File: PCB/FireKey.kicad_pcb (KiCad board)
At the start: 2 copper layers, 100 x 96.5 mm, 75 parts, among them SW1 SW_MEC_4A, U1 Arduino_Pro_Micro_USB-C

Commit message: Worked on V1.0.0 PCB
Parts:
- removed C15: 100nF, Capacitor_SMD:C_0603_1608Metric_Pad1.08x0.95mm_HandSolder
- removed G1: FireKey_Logo, Custom_Parts:FireKey_Logo
- removed H11, H12: M3_Hole, MountingHole:MountingHole_3.2mm_M3
- removed LED15: DY-S352818, Custom_Parts:DY-S352818-6812-2T
- added C0: 100nF, Capacitor_SMD:C_0603_1608Metric_Pad1.08x0.95mm_HandSolder, B.Cu at (231.5, 91.3)
- added LED0: SK6812, Custom_Parts:DY-S352818-6812-2T, B.Cu at (238.8, 92.1)
- added Logo1: Logo_FireKey, Custom_FireKey:Logo_FireKey_32x9.4, F.Cu at (128.9, 162.4)
- added OLED2: OLED_1.3_4P, Custom_Module:OLED_1.3_4P_withM2.5Holes, F.Cu at (207.8, 55.9)
- H1: renamed from H5; value M3_Hole -> M2.5_Hole; footprint MountingHole:MountingHole_3.2mm_M3 -> MountingHole:MountingHole_2.7mm_M2.5
- H2: renamed from H6; value M3_Hole -> M2.5_Hole; footprint MountingHole:MountingHole_3.2mm_M3 -> MountingHole:MountingHole_2.7mm_M2.5
- H3: renamed from H9; value M3_Hole -> M2.5_Hole; footprint MountingHole:MountingHole_3.2mm_M3 -> MountingHole:MountingHole_2.7mm_M2.5
- H4: renamed from H10; value M3_Hole -> M2.5_Hole; footprint MountingHole:MountingHole_3.2mm_M3 -> MountingHole:MountingHole_2.7mm_M2.5
- H5: renamed from H7; value M3_Hole -> M2.5_Hole; footprint MountingHole:MountingHole_3.2mm_M3 -> MountingHole:MountingHole_2.7mm_M2.5
- H6: renamed from H8; value M3_Hole -> M2.5_Hole; footprint MountingHole:MountingHole_3.2mm_M3 -> MountingHole:MountingHole_2.7mm_M2.5
- LED1, LED10, LED11, LED12, LED13, LED14, LED2, LED3, LED4, LED5, LED6, LED7, LED8, LED9: value DY-S352818 -> SK6812
- moved H2 200.3 mm to (248.9, 41.3)
- moved C9 184.9 mm to (246.0, 111.9), turned to 0 degrees
- moved KEY15 170.7 mm to (241.3, 119.4)
- moved D15 170.6 mm to (245.7, 118.1)
- moved LED10 170.3 mm to (238.8, 130.2), turned to 180 degrees
- moved LED9 170.3 mm to (238.8, 111.1), turned to 0 degrees
- moved C10 155.8 mm to (231.5, 129.4), turned to 180 degrees
- moved KEY14 154.4 mm to (241.3, 100.3)
- moved D14 154.4 mm to (245.7, 99.1)
- moved D4 151.3 mm to (226.7, 80.0)
- moved KEY4 151.3 mm to (222.2, 81.3)
- moved C8 146.8 mm to (226.9, 111.9), turned to 0 degrees
- moved KEY13 141.5 mm to (241.3, 81.3)
- moved D13 141.4 mm to (245.7, 80.0)
- moved KEY3 134.5 mm to (203.2, 81.3)
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- renumbered H3 to P1, H2 to P2
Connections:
- D10 pad 1: Row3 -> Row2
- D11 pad 1: Row3 -> Row2
- D12 pad 1: Row3 -> Row2
- D13 pad 1: Row4 -> Row0
- D14 pad 1: Row4 -> Row1
- D15 pad 1: Row4 -> Row2
- D4 pad 1: Row1 -> Row0
- D7 pad 1: Row2 -> Row1
- D8 pad 1: Row2 -> Row1
- KEY1 pad 2: Col0 -> Col4
- KEY10 pad 2: Col2 -> Col3
- KEY11 pad 2: Col1 -> Col2
- KEY12 pad 2: Col0 -> Col1
- KEY14 pad 2: Col1 -> Col0
- KEY15 pad 2: Col2 -> Col0
- KEY2 pad 2: Col1 -> Col3
- KEY4 pad 2: Col2 -> Col1
- KEY5 pad 2: Col1 -> Col4
- KEY6 pad 2: Col0 -> Col3
- KEY7 pad 2: Col0 -> Col2
- KEY9 pad 2: Col2 -> Col4
- LED1 pad 4: Net-(LED1-Pad4) -> Net-(LED0-Pad2)
- LED14 pad 2: Net-(LED14-Pad2) -> unconnected-(LED14-Pad2)
- R1 pad 1: Net-(LED1-Pad4) -> Net-(LED0-Pad4)
- U1 pad 10: Col0 -> Row0
- U1 pad 14: Col2 -> Row2
- U1 pad 16: Col1 -> Row1
- U1 pad 5: Row0 -> Col0
- U1 pad 6: Row1 -> Col1
- U1 pad 7: Row2 -> Col2
- U1 pad 8: Row3 -> Col3
- U1 pad 9: Row4 -> Col4
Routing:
- net VCC: track 575.2 -> 0.00 mm, vias 7 -> 0
- net Col2: track 189.8 -> 0.00 mm
- net Col1: track 169.2 -> 0.00 mm
- net Col0: track 144.6 -> 0.00 mm
- net Row4: track 91.8 -> 0.00 mm
- net Row3: track 73.0 -> 0.00 mm
- net Row0: track 67.2 -> 0.00 mm
- net Row2: track 58.4 -> 0.00 mm
- net Row1: track 56.4 -> 0.00 mm
- net SDA: track 46.6 -> 0.00 mm
- net LEDpin: track 45.2 -> 0.00 mm, vias 1 -> 0
- net SCL: track 42.7 -> 0.00 mm
- net Net-(LED3-Pad2): track 27.2 -> 0.00 mm
- net Net-(LED10-Pad4): track 27.2 -> 0.00 mm
- net Net-(LED6-Pad2): track 26.7 -> 0.00 mm, vias 2 -> 0
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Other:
- board size 100 x 96.5 mm -> 99.7 x 99.1 mm
- board text added: "V1.0"
- board text removed: "V0.1"

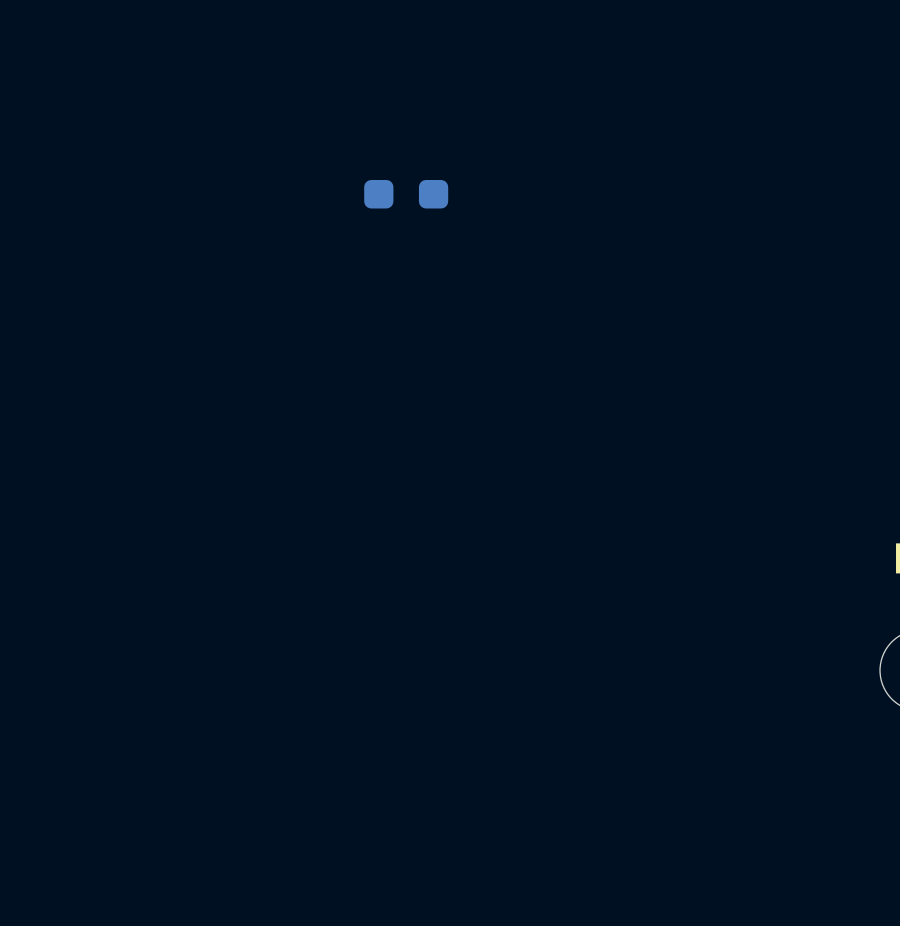
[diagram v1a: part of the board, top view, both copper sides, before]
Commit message: group key sets on pcb
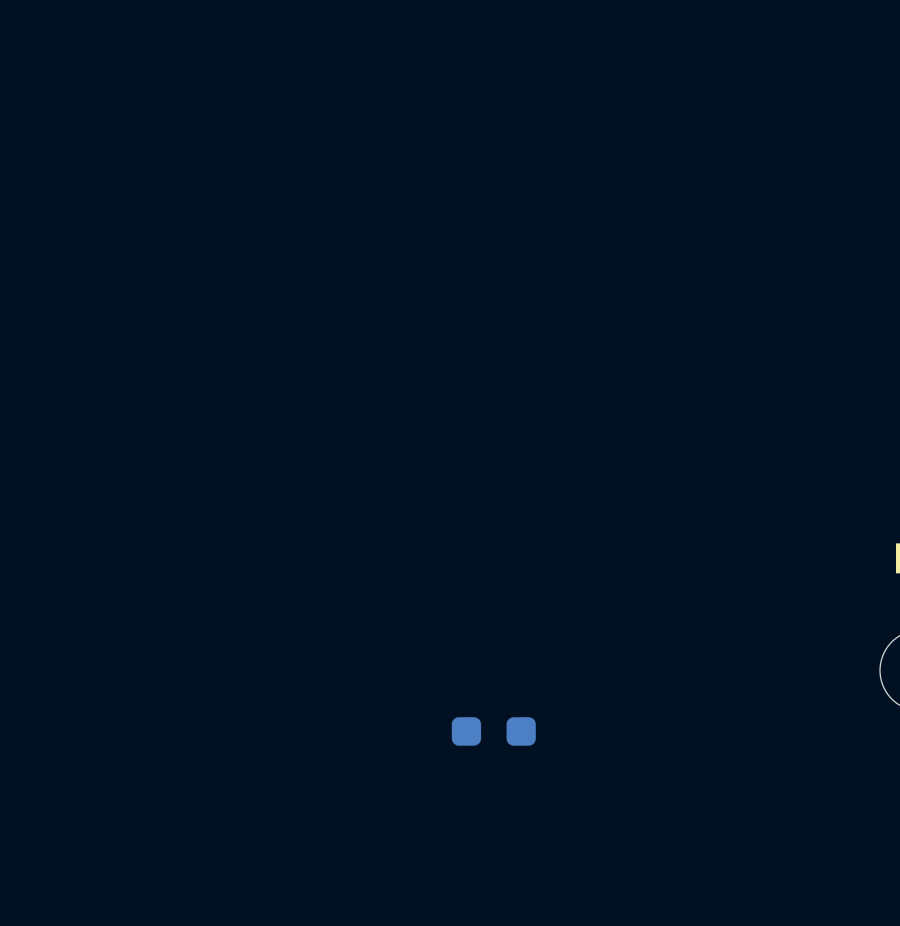
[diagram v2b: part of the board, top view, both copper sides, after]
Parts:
- moved R1 18.1 mm to (84.2, 150.6)
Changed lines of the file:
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@@
   )
   (footprint "Resistor_SMD:R_0603_1608Metric_Pad0.98x0.95mm_HandSolder" (layer "B.Cu")
-    (at 81.28 132.715 180)
+    (at 84.201 150.622 180)
     (descr "Resistor SMD 0603 (1608 Metric), square (rectangular) end terminal, IPC_7351 nominal with elongated pad for handsoldering. (Body size source: IPC-SM-782 page 72, https://www.pcb-3d.com/wordpress/wp-content/uploads/ipc-sm-782a_amendment_1_and_2.pdf), generated with kicad-footprint-generator")
     (tags "resistor handsolder")
@@
     )
   )
+  (group "" (id 0c8eb329-8a7c-4bb5-9813-11b4b3e45d43)
+    (members
+      4b3f97e3-f692-467a-bb9a-6525d59c23be
+      707c6513-1ab0-4c7c-a189-50d838967762
+      7e8e07dc-734d-4172-bba8-4db457fe37e6
+      b4d0023a-42cd-4c26-829e-b9827198be04
+    )
+  )
+  (group "" (id 121ba5f1-8ab7-4999-a983-b4f6366fa974)
+    (members
+      46cfd767-3e17-4856-b877-8c1122b8601d
+      81f56482-9ccc-4496-adac-18be6a31b7a0
+      921472f3-4842-432a-92b4-1a425d50b379
+      c7335970-5a1a-4518-9ef3-074f1f9dd307
+    )
+  )
+  (group "" (id 2e79554f-7390-4ca6-8009-49a1f95f9d67)
+    (members
+      26228caf-224c-4274-b176-32013030fab0
+      38324b1f-14e6-478c-aced-0a1d7548ab23
+      61e89871-909b-4611-a969-187cf2a1b5b8
+      fea4620c-5fa8-4800-99d6-69ae5492dc75
+    )
+  )
+  (group "" (id 3d0f866c-5178-4d1d-8eb4-1fa3dfc1bbc8)
+    (members
+      632036c0-7358-44ae-a0b3-72e0552fbb83
+      6f5881f9-7b76-4aa6-94a5-8e8359a29d25
+      9279b8af-bd90-42a6-84d3-6ab29e055f9b
+      d1424849-b1af-43c3-a3c6-62be62da0825
+    )
+  )
+  (group "" (id 434db756-ec08-4871-a901-14f93056c3d9)
+    (members
+      4b7ab318-8dc2-4af0-90b8-7847eb0e3d18
+      5b0763ea-f79e-46d6-a76e-e23f4f372395
+      60a0e623-08f5-45cd-bcf7-0abda9977d2e
+      bd537039-61eb-449b-92f5-c42de07df635
+    )
+  )
+  (group "" (id 6a048222-94f8-4a41-8778-b92ea910cbb6)
+    (members
+      1df8dcc0-99b1-4d9e-9e96-3ccb71a2016c
+      b7f6fd0f-52f3-4d4f-9611-488a7a775906
+      d504ab76-de17-467e-a2be-6801e51282b5
+      f2a42b1f-1863-4219-bc2e-978af76eb773
+    )
+  )
+  (group "" (id af2262b5-aebd-47c9-b040-323d86d358e6)
+    (members
+      28121cb0-38e4-4f38-bb25-648309b21e2c
+      6e4398f2-582a-4c37-9d53-e9b0b35901df
+      83a0c476-5c87-4a03-9319-f0d5aa272caa
+      ed54c982-ec0f-4aef-b707-ff4224214f5d
+    )
+  )
+  (group "" (id b5407760-221f-4d78-84a1-78707285355b)
+    (members
+      098ae4ba-2664-4e44-9cad-7231985e52a1
+      4b74b7bc-3f4e-4b75-8054-e5d3fad12003
+      5a8270cd-6040-4764-9e04-a32b7e6c86c9
+      e78ab399-ca99-42ce-9cb4-4931e3cbbc71
+    )
+  )
+  (group "" (id b915ce75-a1cf-4f97-b629-b2363b97fc3d)
+    (members
+      862df89c-8478-4ac4-8603-210bda7e1e00
+      8ba72766-558c-4494-b7df-cc41d3f583e7
+      bfe171f7-9438-479c-a44c-46b3886576ce
+      ffd0198b-2d9e-47bf-8d9f-138184743185
+    )
+  )
+  (group "" (id c10fb0a5-a9c5-4c9f-940f-f8aae66fe50f)
+    (members
+      1ffe9b5f-97cd-4317-85fe-b80f4cbdc101
+      2a1a0cf2-ca65-45ce-a672-68f3b03bc522
+      5fb8700b-3a71-4a7d-8dbb-577e558bb866
+      a4919f57-c902-4a2d-9c93-9b108622b5fe
+    )
+  )
+  (group "" (id cbd88b4e-500a-4292-84e9-65deffd97771)
+    (members
+      5bb48020-8cf3-457f-8159-caa61c77082b
+      dcd99bf3-a69a-4ede-8d41-889fa46936bf
+      e2413b90-cb77-481f-bfea-c6a7d6571577
+      e374bbc5-79cf-4037-85aa-8117c14d8d89
+    )
+  )
+  (group "" (id d23a4542-1d42-4acb-8d53-6d6fc1d39a0a)
+    (members
+      3bf5c10c-f476-48bf-baac-ef17de4f26bc
+      969c9d08-53db-4615-9ba0-51aee62ad12d
+      97a6b693-5da5-476a-abdb-37fa277d7349
+      be6af58b-fb7d-4112-9096-56e1908ccb12
+    )
+  )
+  (group "" (id d5d6f00b-df92-4c9f-9eee-214b018f63b9)
+    (members
+      516d1335-f865-4f76-b5a1-0c11b8c59e94
+      5871ae55-1afa-432c-9750-d1f634fbceb9
+      a902c4cf-1eae-4278-b2be-5dcd3a3253c2
+      fdeda7c8-9130-4b94-9f3e-0c76f9b21809
+    )
+  )
+  (group "" (id fc144baf-8b79-4543-835a-01b15aa0a477)
+    (members
+      1eae6c14-31c8-4858-ba9e-bfbd76422ff9
+      96cfe663-e390-487f-b23d-89462acd432c
+      b28aef67-e94c-4ae6-9358-b96fd7ad3e79
+      f9ec8f73-3bd1-4641-b725-d155aef00eec
+    )
+  )
+  (group "" (id ff166843-d988-4a62-a92a-1700fd8a9d57)
+    (members
+      44899f2f-ae88-4c25-9ba9-df4d9a646658
+      510f5677-94b3-4b8b-ac82-c2888fd29e55
+      8ad3ed86-993d-4d82-a765-528d1203db66
+      9fe647a4-61ec-4170-99cd-7748d05132fb
+    )
+  )

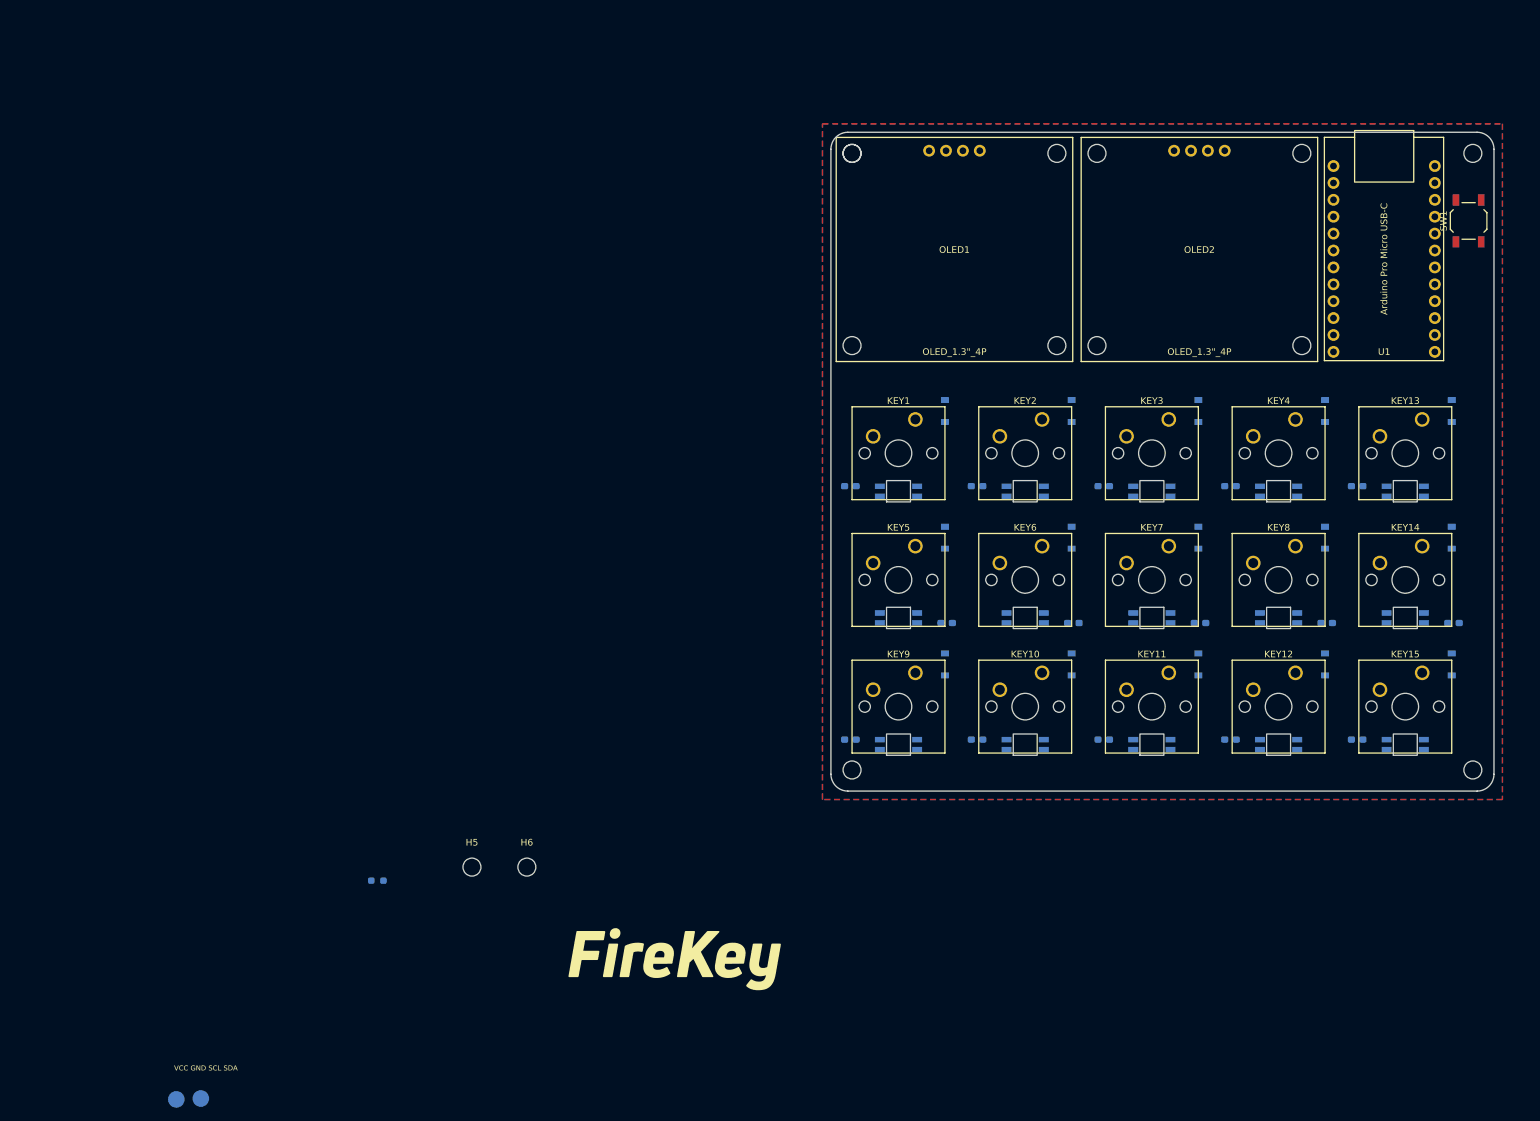
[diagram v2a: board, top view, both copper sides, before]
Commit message: worked on key matrix routing
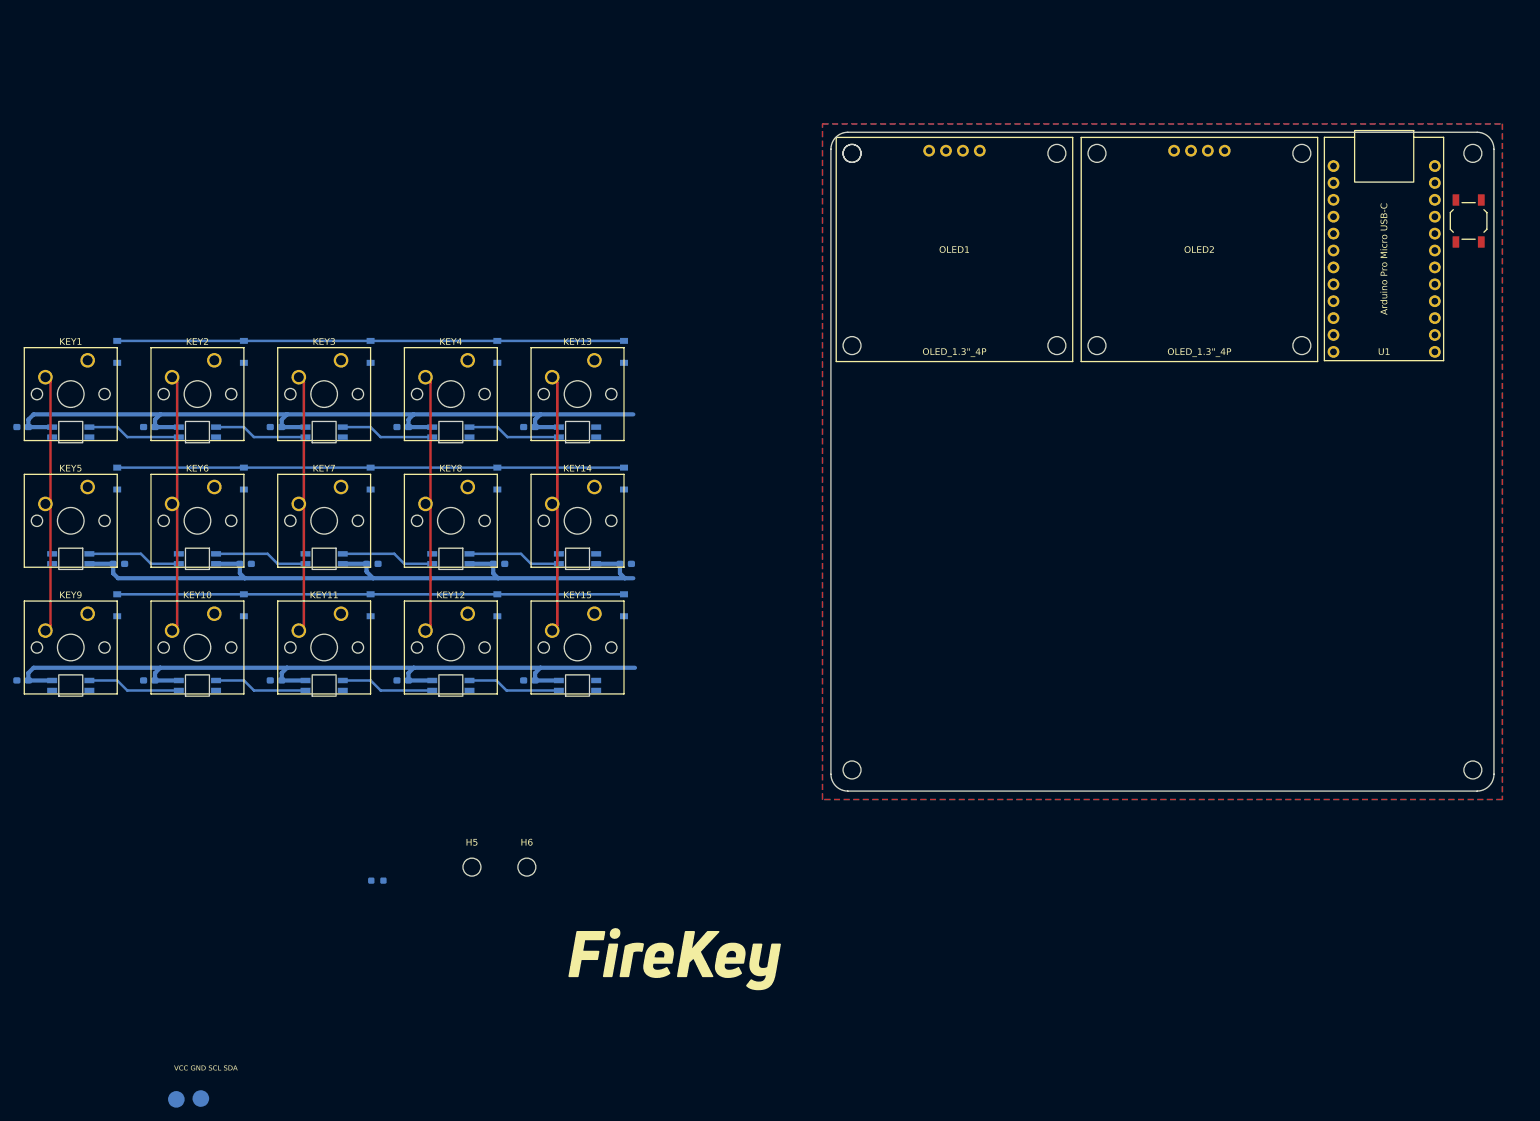
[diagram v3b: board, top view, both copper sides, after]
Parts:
- moved C1 124.8 mm to (88.0, 82.4)
- moved C11 124.8 mm to (88.0, 120.5)
- moved C13 124.8 mm to (49.9, 120.5)
- moved C3 124.8 mm to (49.9, 82.4)
- moved C5 124.8 mm to (45.3, 103.0)
- moved C7 124.8 mm to (83.4, 103.0)
- moved C8 124.8 mm to (102.5, 103.0)
- moved D11 124.8 mm to (83.2, 109.2)
- moved D13 124.8 mm to (121.3, 71.1)
- moved D14 124.8 mm to (121.3, 90.2)
- moved D15 124.8 mm to (121.3, 109.2)
- moved D3 124.8 mm to (83.2, 71.1)
- moved D7 124.8 mm to (83.2, 90.2)
- moved KEY10 124.8 mm to (59.7, 110.5)
- moved KEY13 124.8 mm to (116.8, 72.4)
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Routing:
- net VCC: track 0.00 -> 346.5 mm
- net Row2: track 0.00 -> 76.2 mm
- net Row1: track 0.00 -> 76.2 mm
- net Row0: track 0.00 -> 76.2 mm
- net Col4: track 0.00 -> 38.7 mm
- net Col2: track 0.00 -> 38.7 mm
- net Col1: track 0.00 -> 38.7 mm
- net Col0: track 0.00 -> 38.7 mm
- net Col3: track 0.00 -> 38.7 mm
- net Net-(LED8-Pad2): track 0.00 -> 14.1 mm
- net Net-(LED7-Pad2): track 0.00 -> 14.1 mm
- net Net-(LED6-Pad2): track 0.00 -> 14.1 mm
- net Net-(LED5-Pad2): track 0.00 -> 14.1 mm
- net Net-(LED3-Pad2): track 0.00 -> 14.1 mm
- net Net-(LED2-Pad2): track 0.00 -> 14.1 mm
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
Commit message: worked on pcb routing
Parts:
- moved P1 202.1 mm to (174.9, 21.6)
- moved P2 197.3 mm to (170.3, 21.5)
- moved R1 193.8 mm to (256.5, 62.0), turned to 90 degrees
- moved C12 125.4 mm to (194.1, 129.4)
- moved C2 125.4 mm to (194.1, 91.3)
- moved C6 125.4 mm to (189.5, 111.9)
- moved D12 125.4 mm to (227.3, 118.1)
- moved D4 125.4 mm to (227.3, 80.0)
- moved D8 125.4 mm to (227.3, 99.1)
- moved KEY1 125.4 mm to (165.7, 81.3)
- moved KEY11 125.4 mm to (203.8, 119.4)
- moved KEY3 125.4 mm to (203.8, 81.3)
- moved KEY5 125.4 mm to (165.7, 100.3)
- moved KEY7 125.4 mm to (203.8, 100.3)
- moved KEY9 125.4 mm to (165.7, 119.4)
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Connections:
- U1 pad 5: Col0 -> Col4
- U1 pad 6: Col1 -> Col3
- U1 pad 8: Col3 -> Col1
- U1 pad 9: Col4 -> Col0
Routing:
- net VCC: track 346.5 -> 516.5 mm, vias 0 -> 3
- net Col4: track 38.7 -> 128.2 mm
- net SCL: track 0.00 -> 69.6 mm, vias 0 -> 1
- net Col3: track 38.7 -> 106.6 mm
- net SDA: track 0.00 -> 63.8 mm
- net Row2: track 76.2 -> 135.0 mm
- net Col2: track 38.7 -> 85.0 mm
- net Row1: track 76.2 -> 110.8 mm
- net Col1: track 38.7 -> 65.2 mm
- net Col0: track 38.7 -> 57.1 mm
- net Row0: track 76.2 -> 85.9 mm
- net RST: track 0.00 -> 9.47 mm
- net GND: track 0.00 -> 6.30 mm, vias 0 -> 12
- net Net-(D12-Pad2): track 0.00 -> 4.60 mm
- net Net-(D8-Pad2): track 0.00 -> 4.60 mm
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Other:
- board text added: "RST"

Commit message: worked on PCB tracing and DRC errors
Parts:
- KEY1, KEY10, KEY11, KEY12, KEY13, KEY14, KEY15, KEY2, KEY3, KEY4, KEY5, KEY6, KEY7, KEY8, KEY9: footprint Button_Switch_Keyboard:SW_Cherry_MX_1.00u_PCB -> Custom_Parts:SW_Cherry_MX_1.00u_PCB_CleanFront

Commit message: worked on DRC errors; routing
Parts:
- removed the H1 at (155.6, 41.3)
- removed H5, H6: M2.5_Hole, MountingHole:MountingHole_2.7mm_M2.5
- moved R1 19.7 mm to (242.4, 75.7), turned to 180 degrees
- moved P1 3.91 mm to (174.0, 25.4)
- moved P2 3.91 mm to (169.4, 25.3)
- renumbered H2 to H1, H3 to H2, H4 to H3
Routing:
- net Net-(LED4-Pad2): track 0.00 -> 27.8 mm
- net LEDpin: track 0.00 -> 27.2 mm
- net Net-(LED10-Pad4): track 0.00 -> 27.2 mm, vias 0 -> 2
- net Net-(LED0-Pad4): track 0.00 -> 22.6 mm, vias 0 -> 2
